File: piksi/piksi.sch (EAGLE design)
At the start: 156 parts, among them J1 SMA_EDGE, J6 ZX62-B-5PA, Q1 IRLML6401, U1 6SLX9FTG256, U10 MAX2769, U12 PT7M8206B33TA5EX, U13 M25PX80, U2 LTC3407A_DFN, U3 STM32-M-64-LQFP, U4 7Q-16.368MBG-T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

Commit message: Couple minor mods to schematic
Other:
- note removed: "No STM32F10 compatibility"
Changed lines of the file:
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@@
 <?xml version="1.0" encoding="utf-8"?>
 <!DOCTYPE eagle SYSTEM "eagle.dtd">
-<eagle version="6.2">
+<eagle version="6.3">
 <drawing>
 <settings>
@@
 <description>Microcontroller</description>
 <plain>
-<text x="297.18" y="124.46" size="2.54" layer="111">No STM32F10 compatibility</text>
 <text x="154.94" y="177.8" size="5.08" layer="111">STM32F4 Microcontroller</text>
 <text x="80.01" y="163.83" size="2.54" layer="111">Reset Button</text>
@@
 <plain>
 <text x="182.88" y="91.44" size="2.54" layer="94">1V2</text>
-<text x="7.62" y="78.74" size="1.778" layer="111">Route FB lines away from SW lines so they don't feedback</text>
+<text x="38.1" y="73.66" size="1.778" layer="111">Route FB lines away from
+SW lines so they don't feedback</text>
 <text x="69.85" y="91.44" size="2.54" layer="94">3V3</text>
 <text x="99.695" y="125.095" size="3.81" layer="111">Digital 3V3 / 1V2 Power Rails</text>
@@
 </schematic>
 </drawing>
+<compatibility>
+<note version="6.3" minversion="6.2.2" severity="warning">
+Since Version 6.2.2 text objects can contain more than one line,
+which will not be processed correctly with this version.
+</note>
+</compatibility>
 </eagle>

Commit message: Changed some text that looked weird in the pdf
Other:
- note added: "Route FB lines away from SW"
- note added: "lines so they don't feedback"
- note removed: "Route FB lines away from SW lines so they don't feedback"
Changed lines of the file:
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@@
 <?xml version="1.0" encoding="utf-8"?>
 <!DOCTYPE eagle SYSTEM "eagle.dtd">
-<eagle version="6.3">
+<eagle version="6.2">
 <drawing>
 <settings>
@@
 <plain>
 <text x="182.88" y="91.44" size="2.54" layer="94">1V2</text>
-<text x="38.1" y="73.66" size="1.778" layer="111">Route FB lines away from
-SW lines so they don't feedback</text>
+<text x="38.1" y="78.74" size="1.778" layer="111">Route FB lines away from SW</text>
 <text x="69.85" y="91.44" size="2.54" layer="94">3V3</text>
 <text x="99.695" y="125.095" size="3.81" layer="111">Digital 3V3 / 1V2 Power Rails</text>
@@
 <text x="217.805" y="20.32" size="1.778" layer="111">Digital Power Rails</text>
 <text x="248.285" y="5.08" size="1.778" layer="111">v2.3.1</text>
+<text x="38.1" y="76.2" size="1.778" layer="111">lines so they don't feedback</text>
 </plain>
 <instances>
@@
 </schematic>
 </drawing>
-<compatibility>
-<note version="6.3" minversion="6.2.2" severity="warning">
-Since Version 6.2.2 text objects can contain more than one line,
-which will not be processed correctly with this version.
-</note>
-</compatibility>
 </eagle>

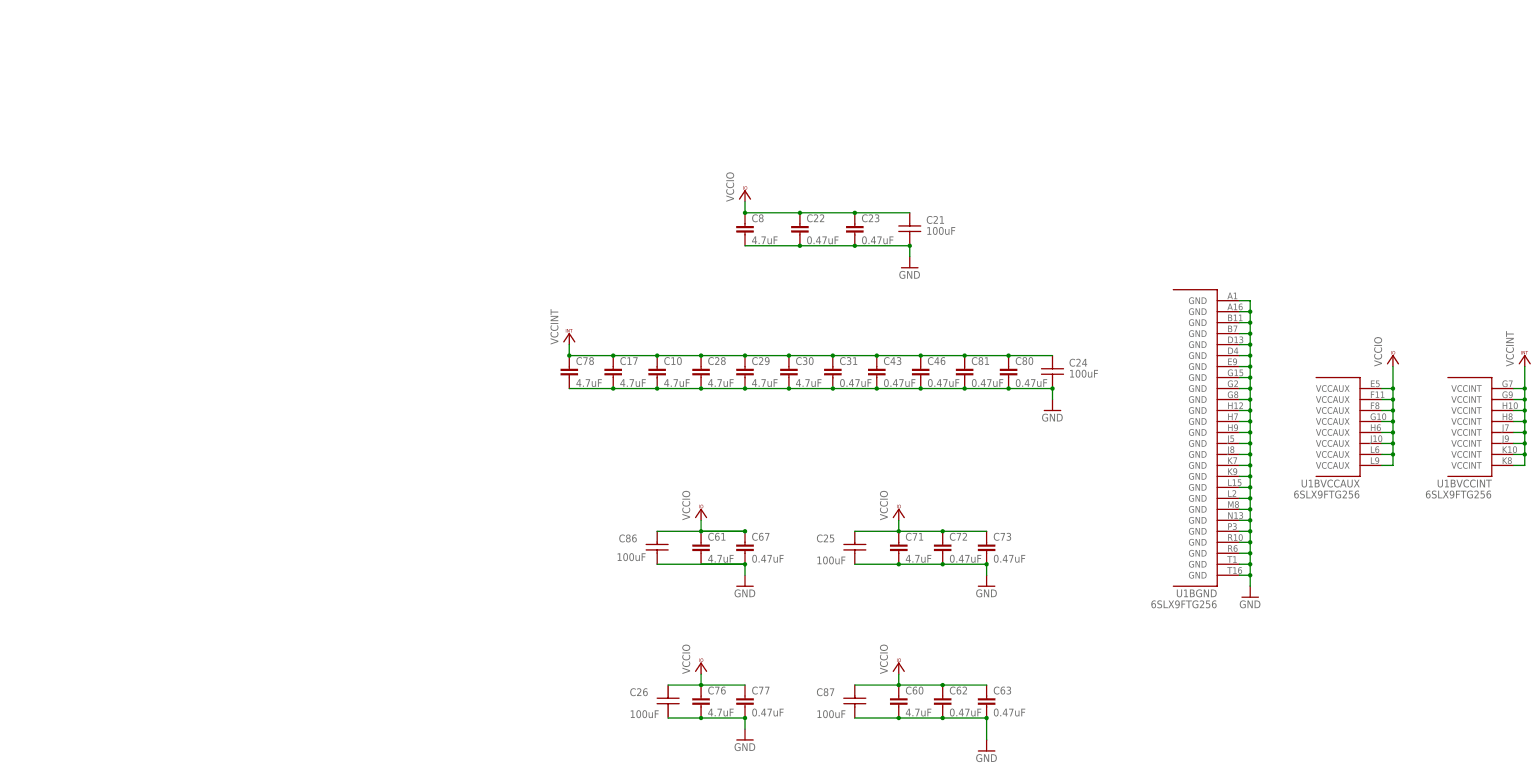
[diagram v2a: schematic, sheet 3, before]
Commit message: Changed A4 frames to A3
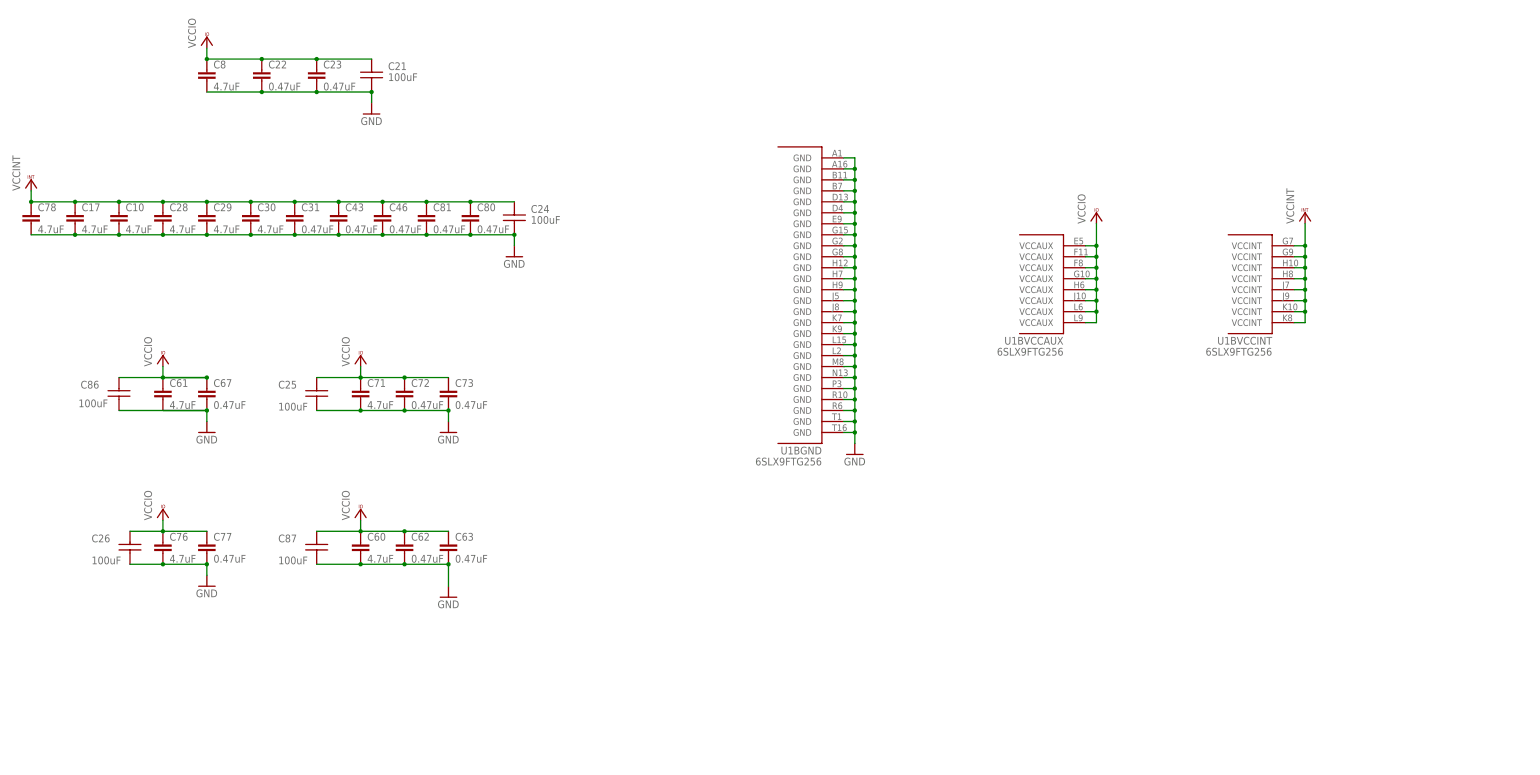
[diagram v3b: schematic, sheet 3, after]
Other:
- note added: "Ground Pins"
- note added: "JTAG chain (for reference)"
- note added: "Spartan 6 Power Bypassing"
- note added: "Spartan 6 Power Pins"
- note added: "VCCAUX Pins"
- note added: "VCCINT Pins"
- note removed: "JTAG chain"
- moved on the sheet: C1, C10, C17, C2, C21, C22, C23, C24, C25, C26, C28, C29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
